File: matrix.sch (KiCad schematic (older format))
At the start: 56 parts

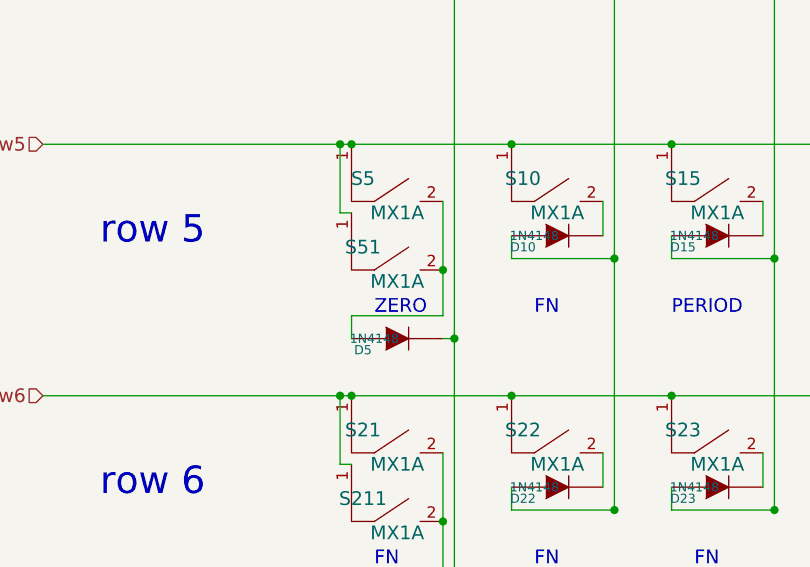
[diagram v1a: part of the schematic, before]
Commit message: Fixed silkscreen
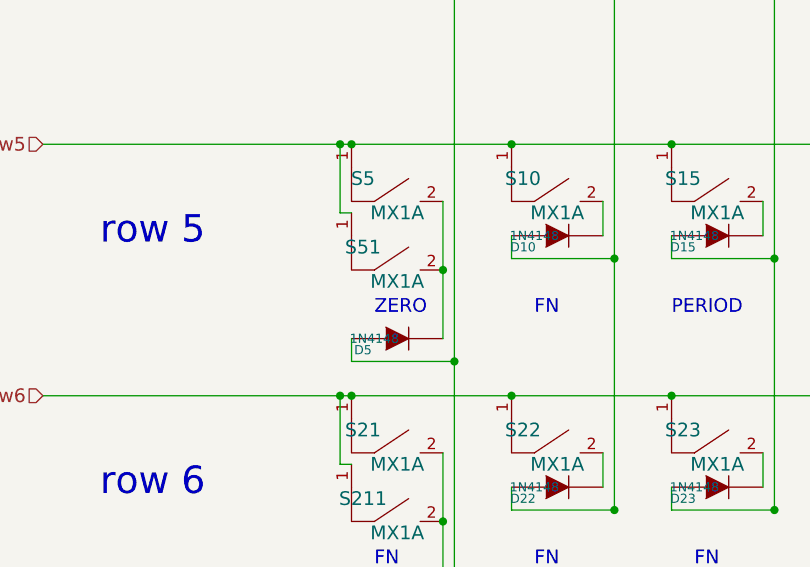
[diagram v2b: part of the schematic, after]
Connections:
- net col1: now also D5.1 (A); no longer D5.2 (K)
- net at S5.2, S51.2: now also D5.2 (K); no longer D5.1 (A)
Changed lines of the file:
@@
-EESchema Schematic File Version 2  date 1/1/2014 1:42:54 PM
+EESchema Schematic File Version 2  date 1/1/2014 8:21:45 PM
 LIBS:power
 LIBS:mx1a-simple
@@
 Sheet 2 2
 Title "4x6 keypad"
-Date "25 nov 2013"
+Date "2 jan 2014"
 Rev "0.12.2"
 Comp "regack"
@@
 Connection ~ 4300 8600
 Wire Wire Line
-	3550 8350 3550 8850
+	3550 8350 3550 8950
 $Comp
 L MX1A S20
@@
 	1    0    0    -1
 $EndComp
-Wire Wire Line
-	3550 8850 3150 8850
-Wire Wire Line
-	3150 8850 3150 8950
-Wire Wire Line
-	3550 8950 3600 8950
-Connection ~ 3600 8950
 Connection ~ 3100 8100
 $Comp
@@
 Text Notes 7300 4600 0    120  ~ 0
 Resistor Value dependent upon LED value
+Wire Wire Line
+	3150 8950 3150 9050
+Wire Wire Line
+	3150 9050 3600 9050
+Connection ~ 3600 9050
 $EndSCHEMATC
